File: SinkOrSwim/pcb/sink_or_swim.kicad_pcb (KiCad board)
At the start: 2 copper layers, 0 parts

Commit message: Footprints associated and parts on pcb
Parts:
- added C201: C, Capacitors_SMD:C_0805_HandSoldering, F.Cu at (177.7, 108.7)
- added C301: C, Capacitors_SMD:C_0805_HandSoldering, F.Cu at (174.5, 139.7)
- added C401: C, Capacitors_SMD:C_0805_HandSoldering, F.Cu at (205.7, 115.1)
- added C402: C, Capacitors_SMD:C_0805_HandSoldering, F.Cu at (200.3, 108.7)
- added D301: DIODE, Diodes_SMD:Diode-SMA_Handsoldering, F.Cu at (162.1, 135.0)
- added P101: CONN_01X02, Pin_Headers:Pin_Header_Straight_1x02, F.Cu at (186.6, 133.5)
- added P102: CONN_01X03, Pin_Headers:Pin_Header_Straight_1x03, F.Cu at (186.6, 138.6)
- added P103: CONN_01X02, Pin_Headers:Pin_Header_Straight_1x02, F.Cu at (197.0, 133.5)
- added Q201: BUK9575-100A, Transistors_TO-220:TO-220_FET-GDS_Vertical, F.Cu at (156.1, 121.6)
- added R201: R, Resistors_SMD:R_0805_HandSoldering, F.Cu at (177.8, 115.1)
- added R202: 1K, Resistors_SMD:R_0805_HandSoldering, F.Cu at (182.9, 108.7)
- added R203: .1, Resistors_ThroughHole:Resistor_Horizontal_RM15mm, F.Cu at (158.6, 110.3)
- added R301: R, Resistors_SMD:R_0805_HandSoldering, F.Cu at (169.3, 133.3)
- added R302: 9K, Resistors_SMD:R_0805_HandSoldering, F.Cu at (169.3, 139.7)
- added R303: 1K, Resistors_SMD:R_0805_HandSoldering, F.Cu at (174.6, 133.3)
- added R401: R, Resistors_SMD:R_0805_HandSoldering, F.Cu at (200.4, 115.1)
- added R402: 27K, Resistors_SMD:R_0805_HandSoldering, F.Cu at (205.6, 108.7)
- added R403: 21.6K, Resistors_SMD:R_0805_HandSoldering, F.Cu at (210.9, 108.7)
- added RV201: POT, pcb:Potiometer_Bourns_3362P, F.Cu at (167.9, 115.9)
- added RV301: POT, pcb:Potiometer_Bourns_3362P, F.Cu at (150.4, 140.5)
- added U201: LMV358, SMD_Packages:SOIC-8-N, F.Cu at (165.5, 122.4)
- added U401: LM2931, SMD_Packages:SOIC-8-N, F.Cu at (194.5, 109.4)

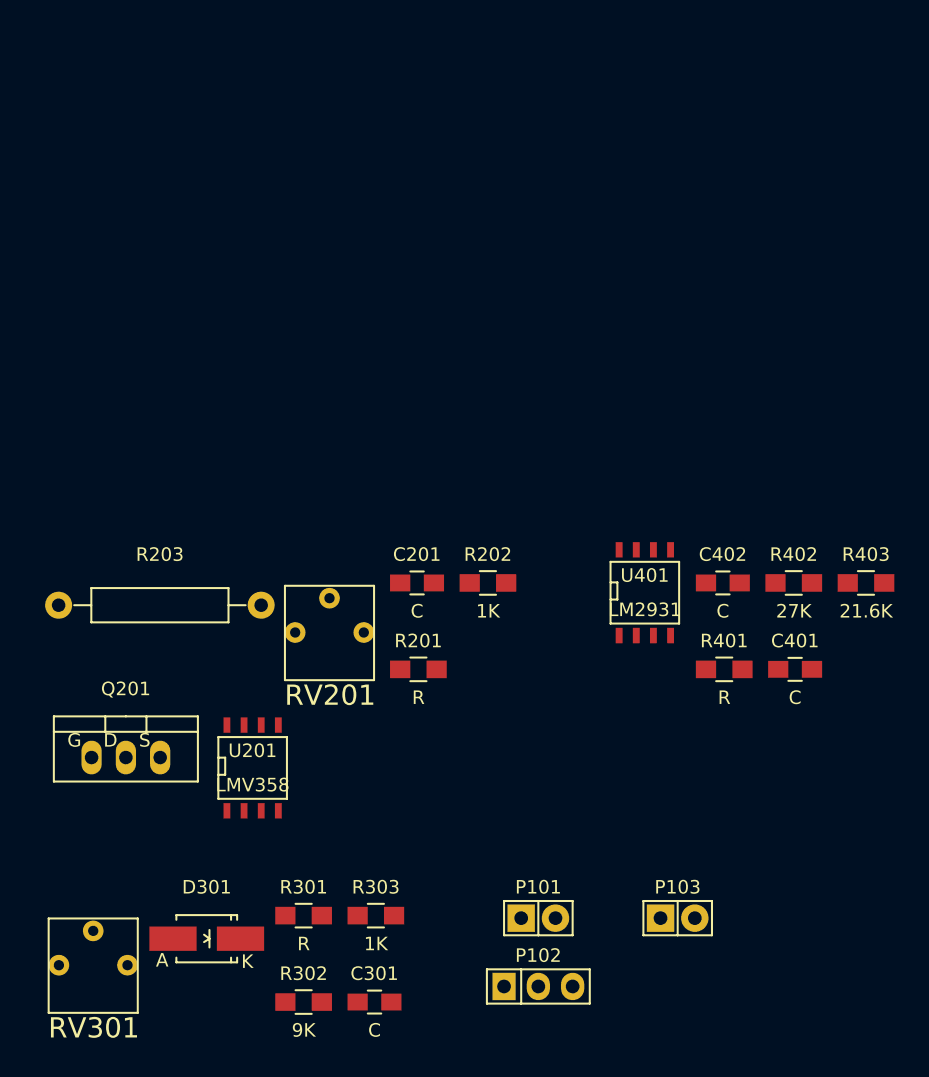
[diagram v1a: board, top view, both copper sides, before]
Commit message: Finished heatsink footprint and first stab at pcb layout.
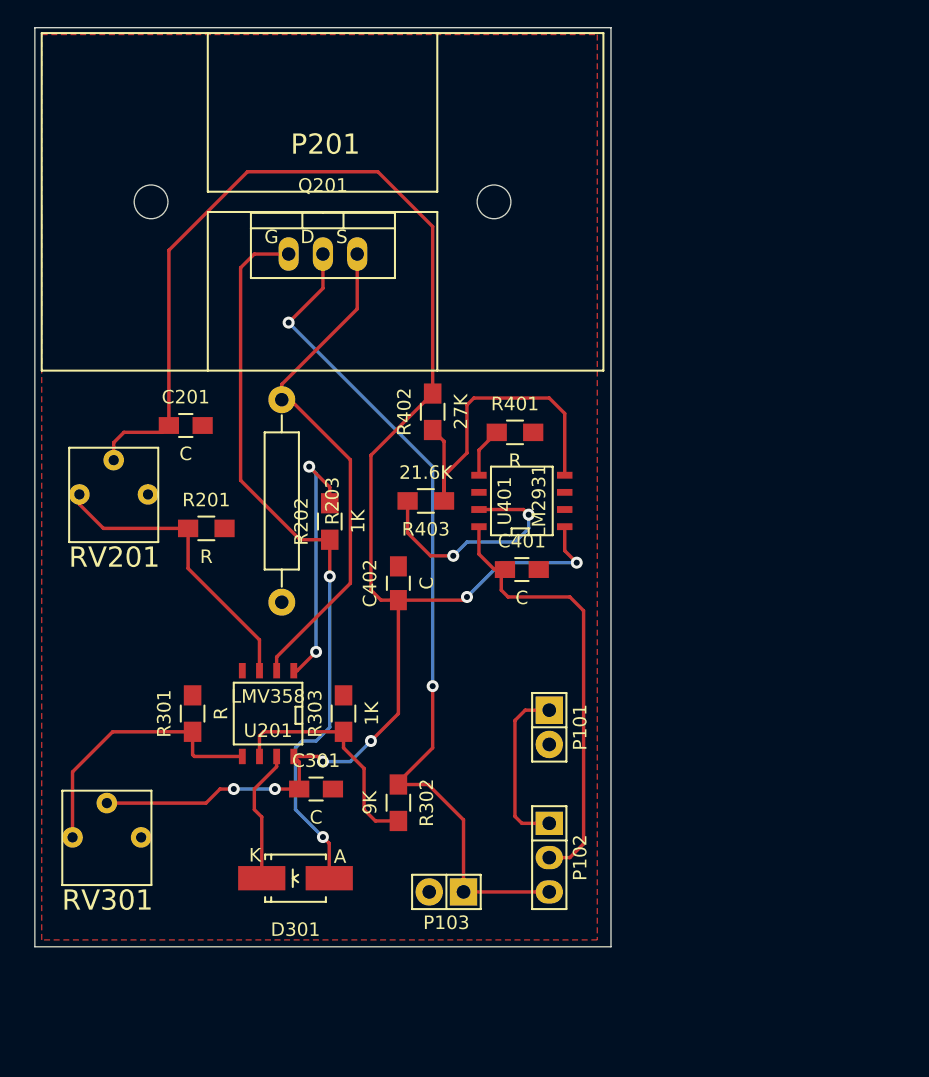
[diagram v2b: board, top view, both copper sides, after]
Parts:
- added P201: CONN_01X01, pcb:FA-T220-38E, F.Cu at (149.9, 93.0)
- moved Q201 40.0 mm to (170.7, 84.3)
- moved R403 33.2 mm to (178.3, 102.6), turned to 180 degrees
- moved R402 29.6 mm to (178.8, 96.0), turned to 90 degrees
- moved C402 24.0 mm to (176.3, 108.7), turned to 90 degrees
- moved R401 23.4 mm to (184.9, 97.5)
- moved C401 21.5 mm to (185.4, 107.7)
- moved C201 20.7 mm to (160.5, 97.0)
- moved RV201 19.0 mm to (151.9, 105.7)
- moved R201 18.9 mm to (162.1, 104.6)
- moved P103 17.2 mm to (179.8, 131.6), turned to 180 degrees
- moved R301 17.1 mm to (161.0, 118.4), turned to 90 degrees
- moved C301 16.4 mm to (170.2, 124.0)
- moved R302 16.3 mm to (176.3, 125.0), turned to 270 degrees
- moved R303 15.2 mm to (172.2, 118.4), turned to 90 degrees
- moved P101 14.2 mm to (187.5, 119.4), turned to 270 degrees
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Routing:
- net 2.7V: track 0.00 -> 126.1 mm, vias 0 -> 6
- net /CurrentControl/Current_Sink+: track 0.00 -> 63.4 mm, vias 0 -> 2
- net /CurrentControl/FET_Gate: track 0.00 -> 55.9 mm, vias 0 -> 2
- net Net-(Q201-PadS): track 0.00 -> 37.9 mm
- net /Power Regulation/Vin: track 0.00 -> 33.0 mm
- net Net-(R402-Pad1): track 0.00 -> 25.9 mm
- net Net-(R201-Pad1): track 0.00 -> 22.3 mm
- net Net-(R301-Pad1): track 0.00 -> 20.4 mm
- net Net-(R202-Pad2): track 0.00 -> 19.5 mm, vias 0 -> 2
- net GND: track 0.00 -> 17.7 mm, vias 0 -> 2
- net Net-(R302-Pad2): track 0.00 -> 17.2 mm
- net Net-(P101-Pad1): track 0.00 -> 12.7 mm
- net Net-(D301-Pad2): track 0.00 -> 9.93 mm
- net Net-(R401-Pad1): track 0.00 -> 3.72 mm
- added copper zone on F.Cu, net GND
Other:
- board outline added: 42.7 x 68.1 mm

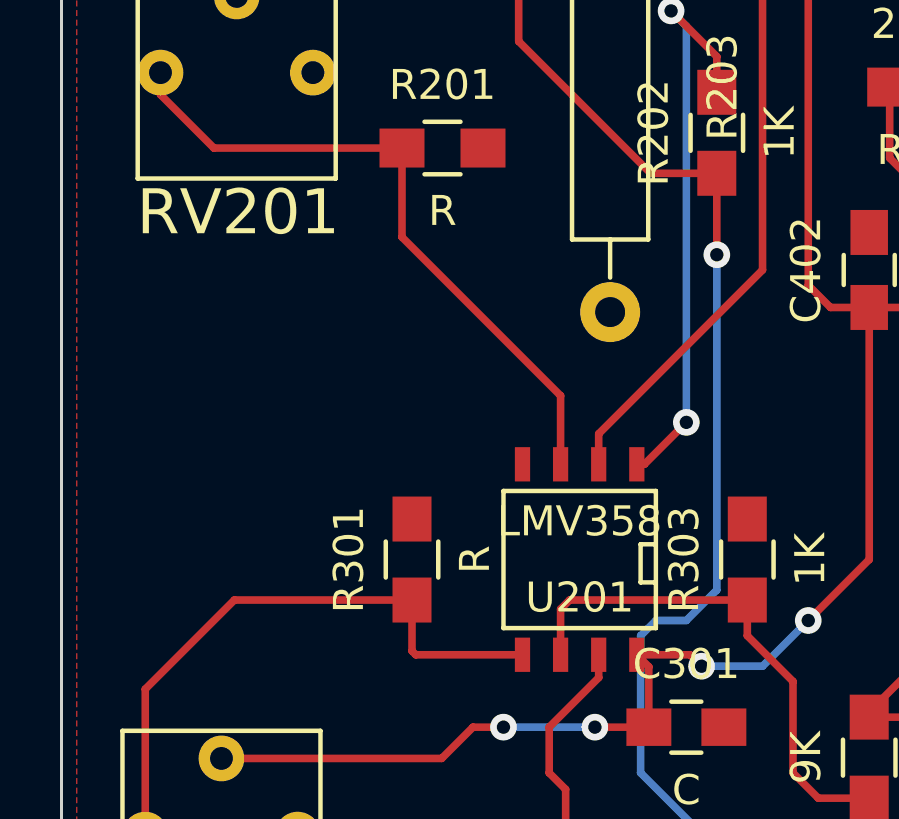
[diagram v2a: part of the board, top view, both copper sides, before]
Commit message: Find new terminal blocks.  Set resistor divider values.  Rearrange POT and fixed resistor.
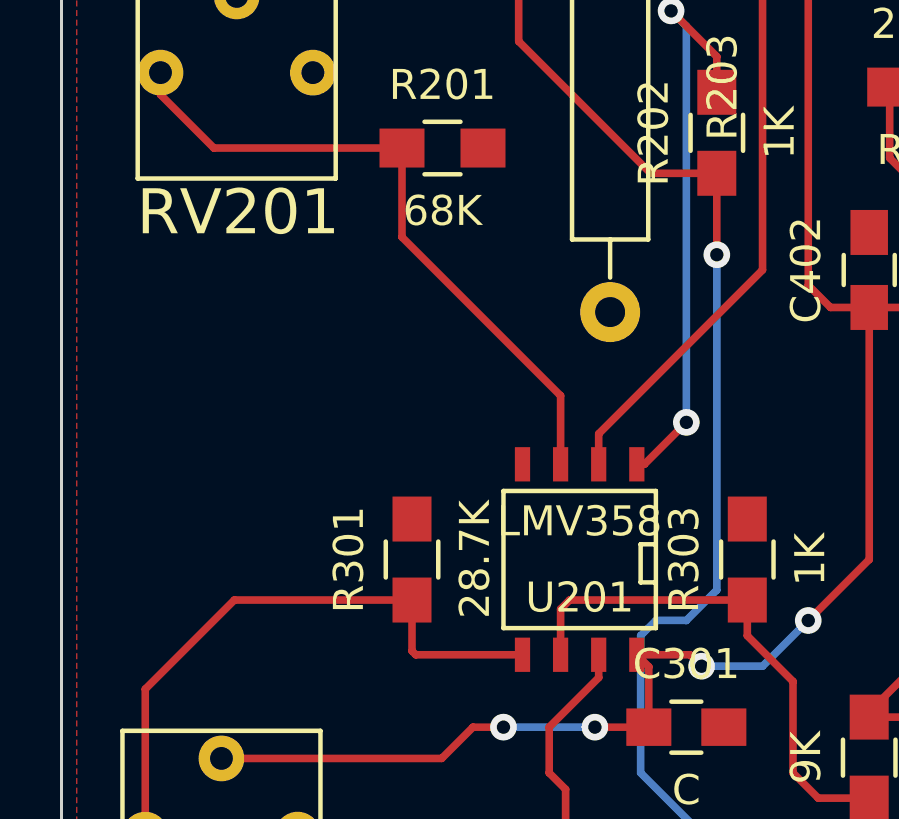
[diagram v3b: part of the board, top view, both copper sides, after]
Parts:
- R201: value R -> 68K
- R301: value R -> 28.7K
- RV201, RV301: value POT -> 10K
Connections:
- R201 pad 1: Net-(R201-Pad1) -> 2.7V
- R201 pad 2: GND -> Net-(R201-Pad2)
- R301 pad 1: Net-(R301-Pad1) -> 2.7V
- R301 pad 2: GND -> Net-(R301-Pad2)
- RV201 pad 2: 2.7V -> Net-(R201-Pad2)
- RV201 pad 3: Net-(R201-Pad1) -> GND
- RV301 pad 2: 2.7V -> Net-(R301-Pad2)
- RV301 pad 3: Net-(R301-Pad1) -> GND
- U201 pad 3: Net-(R201-Pad1) -> Net-(R201-Pad2)
- U201 pad 5: Net-(R301-Pad1) -> Net-(R301-Pad2)
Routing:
- net Net-(R201-Pad1): track 22.3 -> 0.00 mm
- net Net-(R301-Pad1): track 20.4 -> 0.00 mm
- net Net-(R301-Pad2): track 0.00 -> 16.4 mm, vias 0 -> 2
- net GND: track 17.7 -> 30.0 mm
- net Net-(R201-Pad2): track 0.00 -> 12.1 mm
- net 2.7V: track 126.1 -> 127.9 mm, vias 6 -> 4

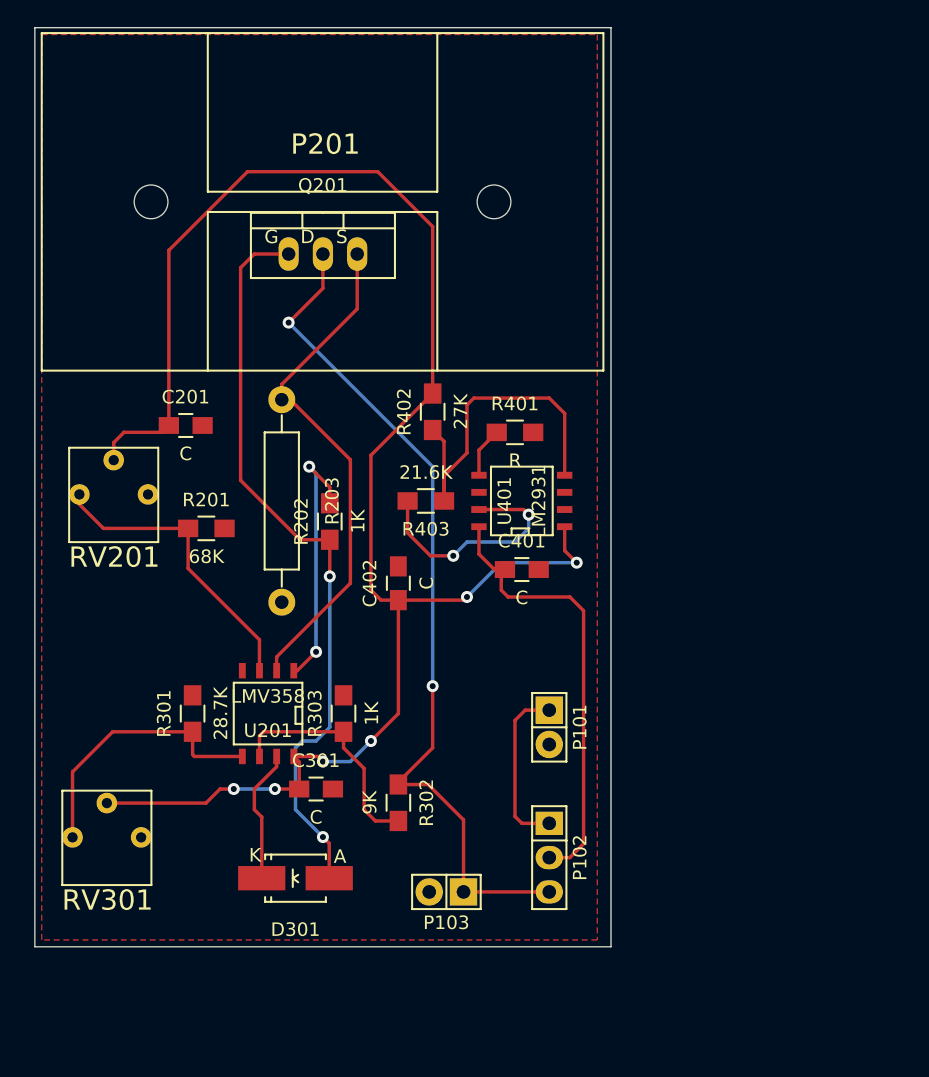
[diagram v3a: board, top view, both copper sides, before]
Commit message: Switched pin headers for terminal blocks for batt and self-powered from sink.  PCB is WIP.
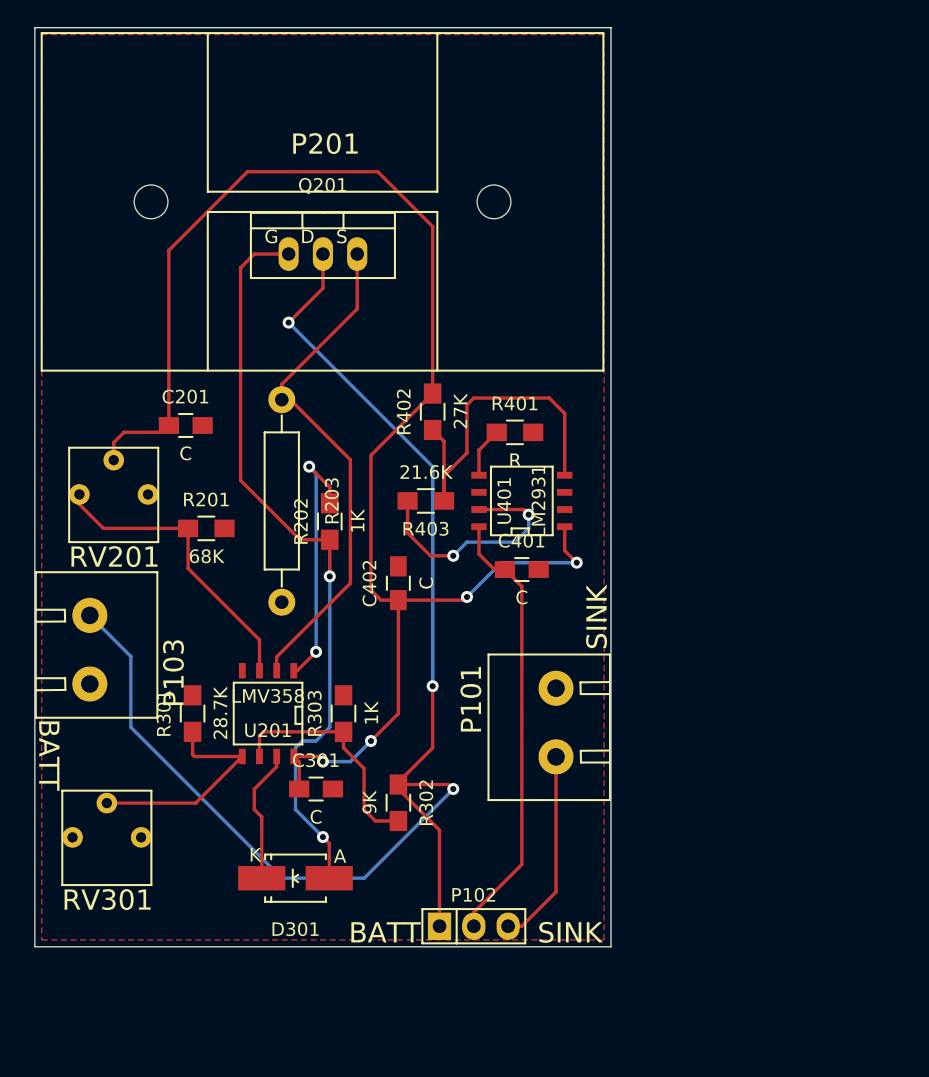
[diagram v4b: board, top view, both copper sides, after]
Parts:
- P101, P103: footprint Pin_Headers:Pin_Header_Straight_1x02 -> pcb:OSTTA024163
- moved P103 31.7 mm to (153.9, 113.3), turned to 270 degrees
- moved P102 7.55 mm to (181.9, 134.1), turned to 0 degrees
- turned P101 to 90 degrees
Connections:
- P102 pad 1: Net-(P101-Pad1) -> /CurrentControl/Current_Sink+
- P102 pad 3: /CurrentControl/Current_Sink+ -> Net-(P101-Pad1)
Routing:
- net /CurrentControl/Current_Sink+: track 63.4 -> 102.6 mm, vias 2 -> 3
- net GND: track 30.0 -> 21.0 mm
- net Net-(R201-Pad2): track 12.1 -> 3.58 mm
- net Net-(P101-Pad1): track 12.7 -> 14.6 mm
- net Net-(R301-Pad2): track 16.4 -> 15.0 mm, vias 2 -> 0
- net 2.7V: track 127.9 -> 128.7 mm
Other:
- board text added: "BATT"
- board text added: "SINK"

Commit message: Small layout changes.
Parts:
- moved C301 3.39 mm to (170.9, 127.3)
- moved D301 2.74 mm to (167.6, 133.1)
- turned R301 to 180 degrees
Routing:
- net Net-(R201-Pad2): track 3.58 -> 30.7 mm, vias 0 -> 2
- net Net-(R301-Pad2): track 15.0 -> 20.2 mm
- net 2.7V: track 128.7 -> 131.7 mm, vias 4 -> 6
- net Net-(D301-Pad2): track 9.93 -> 12.5 mm
- net GND: track 21.0 -> 18.5 mm
- net /CurrentControl/FET_Gate: track 55.9 -> 58.2 mm

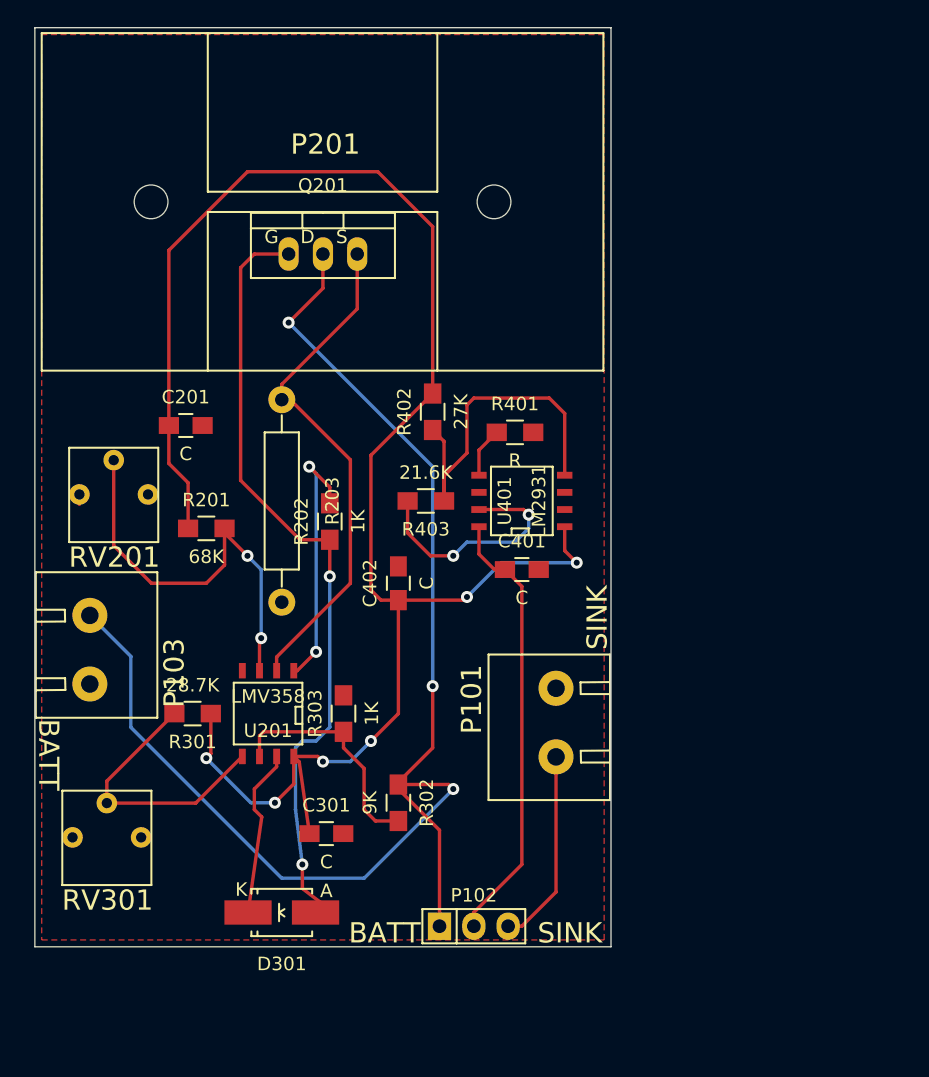
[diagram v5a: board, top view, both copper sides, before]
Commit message: Hide some of the labels on the pcb.  Moved the ground plane to the bottom.  More work reconnecting to do.
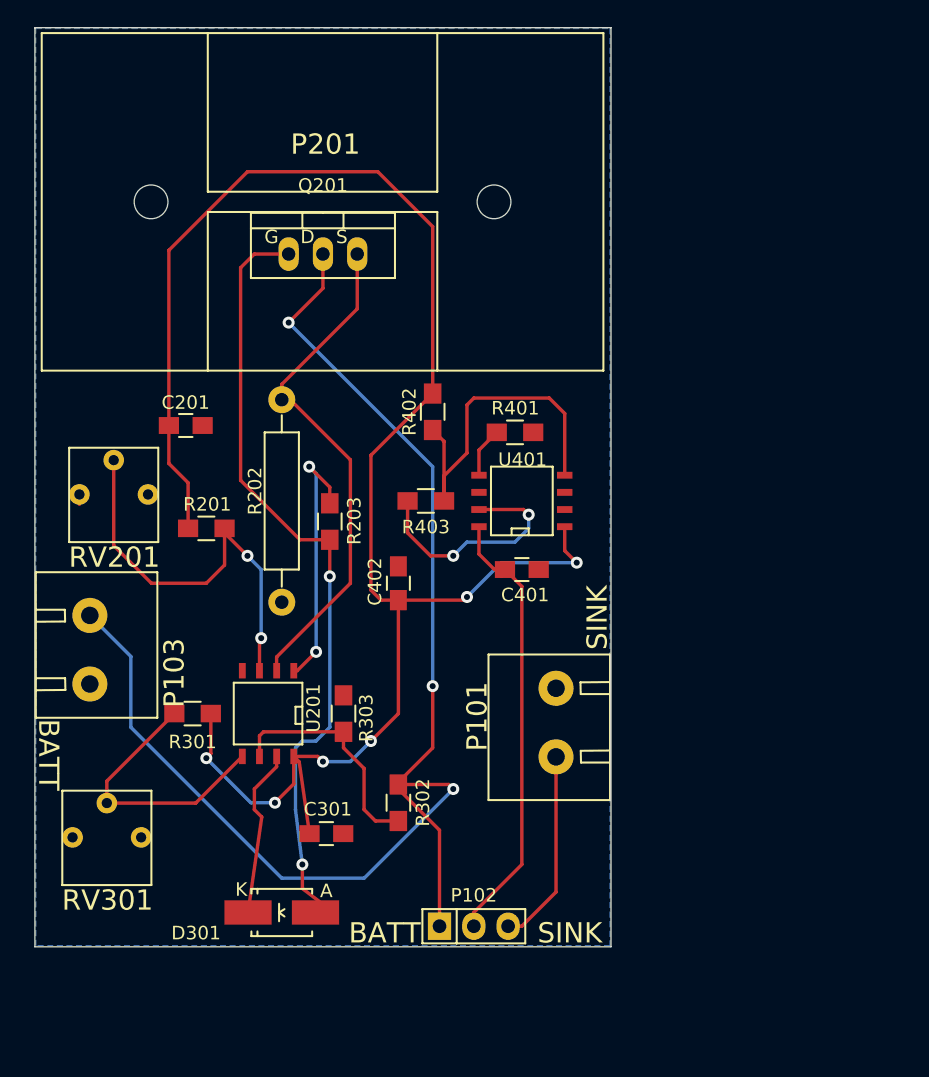
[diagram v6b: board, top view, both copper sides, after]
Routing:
- added copper zone on B.Cu, net GND
- removed copper zone on F.Cu, net GND
